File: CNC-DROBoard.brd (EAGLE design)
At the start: 99.1 x 85.1 mm, 50 parts, among them IC1 ATTINY2313A-PU, IC2 MAX7219CNG, IC3 MAX7219CNG, IC4 74HCT4053P

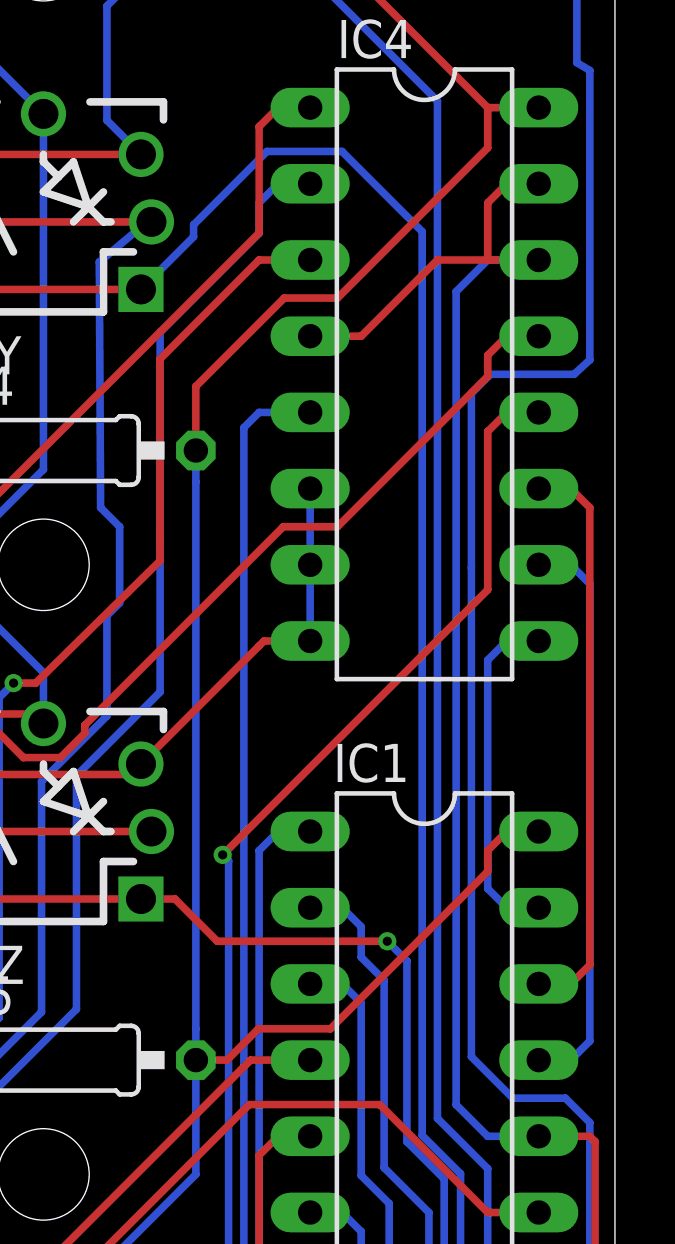
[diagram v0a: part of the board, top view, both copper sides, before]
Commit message: BUGFIX: 74LS4053 doesn't have the commons where you'd think it has - misleading symbol helped me mistake select inputs for common outputs - updated schematic, PCB update pending - this is probably not reworkable on a populated PCB. Will investigate reworkability of a blank PCB - contingency: dead-bug tehnique for the 4053 and onwards we go.
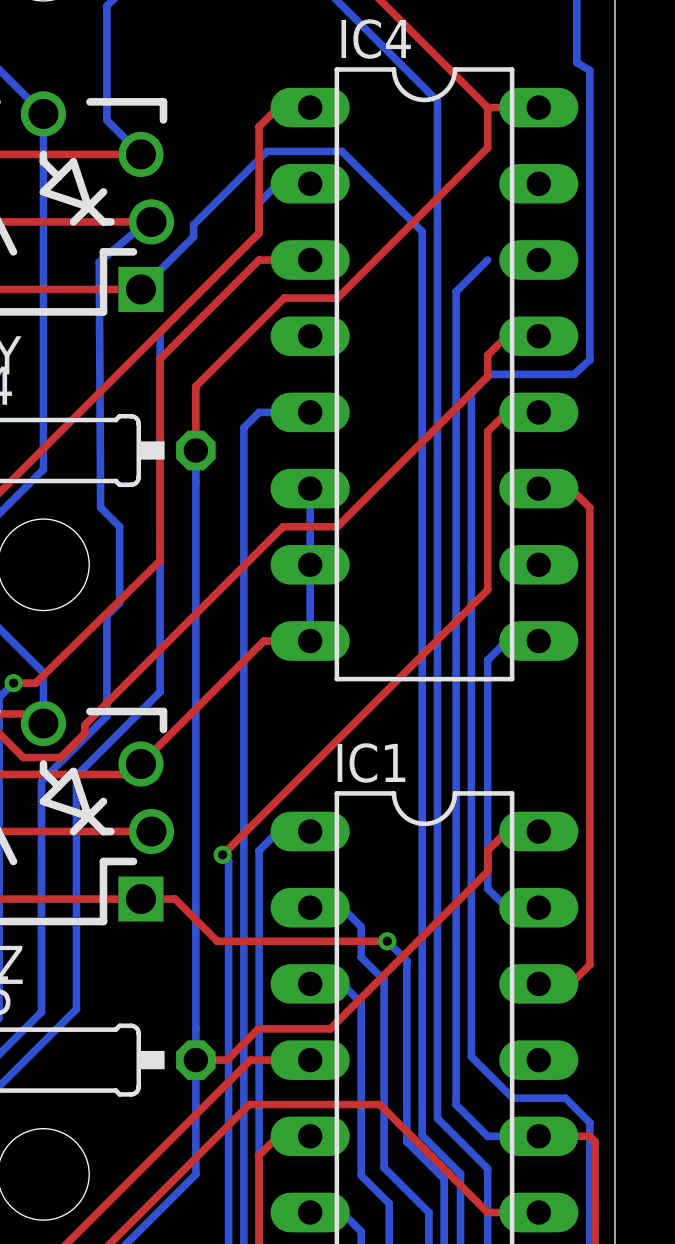
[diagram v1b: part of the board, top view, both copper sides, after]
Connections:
- net !SS: now also IC4.10, IC4.11, IC4.9; no longer IC4.14, IC4.15, IC4.4
- net MISO_INT: now also IC4.14; no longer IC4.11
- net MOSI_INT: now also IC4.15; no longer IC4.10
- net SCK_INT: now also IC4.4; no longer IC4.9
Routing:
- net MOSI_INT: track 19.2 -> 0.00 mm
- net !SS: track 96.5 -> 82.3 mm
- net MISO_INT: track 19.2 -> 18.1 mm
- net SCK_INT: track 11.5 -> 10.5 mm
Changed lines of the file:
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@@
 <?xml version="1.0" encoding="utf-8"?>
 <!DOCTYPE eagle SYSTEM "eagle.dtd">
-<eagle version="6.3">
+<eagle version="6.4">
 <drawing>
 <settings>
@@
 <contactref element="JBUS" pad="3"/>
 <contactref element="IC1" pad="16"/>
-<contactref element="IC4" pad="14"/>
-<contactref element="IC4" pad="15"/>
-<contactref element="IC4" pad="4"/>
 <wire x1="96.52" y1="22.86" x2="98.2219" y2="22.86" width="0.254" layer="1"/>
 <wire x1="71.12" y1="2.54" x2="72.4635" y2="1.1965" width="0.254" layer="1"/>
@@
 <wire x1="98.3977" y1="2.4874" x2="98.3977" y2="22.6842" width="0.254" layer="1"/>
 <wire x1="98.3977" y1="22.6842" x2="98.2219" y2="22.86" width="0.254" layer="1"/>
-<wire x1="96.52" y1="52.07" x2="94.8181" y2="52.07" width="0.254" layer="16"/>
 <wire x1="96.52" y1="22.86" x2="94.8181" y2="22.86" width="0.254" layer="16"/>
 <wire x1="94.8181" y1="22.86" x2="93.7656" y2="23.9125" width="0.254" layer="16"/>
 <wire x1="93.7656" y1="23.9125" x2="93.7656" y2="51.0175" width="0.254" layer="16"/>
 <wire x1="93.7656" y1="51.0175" x2="94.8181" y2="52.07" width="0.254" layer="16"/>
-<wire x1="94.8181" y1="52.07" x2="93.1419" y2="52.07" width="0.254" layer="1"/>
-<wire x1="93.1419" y1="52.07" x2="90.6019" y2="49.53" width="0.254" layer="1"/>
-<wire x1="96.52" y1="52.07" x2="94.8181" y2="52.07" width="0.254" layer="1"/>
-<wire x1="96.52" y1="54.61" x2="95.4531" y2="54.61" width="0.254" layer="1"/>
-<wire x1="95.4531" y1="54.61" x2="94.8181" y2="53.975" width="0.254" layer="1"/>
-<wire x1="94.8181" y1="53.975" x2="94.8181" y2="52.07" width="0.254" layer="1"/>
-<wire x1="88.9" y1="49.53" x2="90.6019" y2="49.53" width="0.254" layer="1"/>
+<contactref element="IC4" pad="9"/>
+<contactref element="IC4" pad="10"/>
+<contactref element="IC4" pad="11"/>
+<wire x1="96.52" y1="41.91" x2="96.52" y2="44.45" width="0" layer="19" extent="1-1"/>
+<wire x1="96.52" y1="39.37" x2="96.52" y2="41.91" width="0" layer="19" extent="1-1"/>
+<wire x1="93.7656" y1="51.0175" x2="96.52" y2="44.45" width="0" layer="19" extent="16-16"/>
 </signal>
 <signal name="!RESET">
@@
 <signal name="SCK_INT">
 <contactref element="IC1" pad="19"/>
-<contactref element="IC4" pad="9"/>
 <wire x1="94.8181" y1="38.735" x2="94.8181" y2="31.115" width="0.254" layer="16"/>
 <wire x1="94.8181" y1="31.115" x2="95.4531" y2="30.48" width="0.254" layer="16"/>
 <wire x1="95.4531" y1="30.48" x2="96.52" y2="30.48" width="0.254" layer="16"/>
-<wire x1="96.52" y1="39.37" x2="95.4531" y2="39.37" width="0.254" layer="16"/>
 <wire x1="95.4531" y1="39.37" x2="94.8181" y2="38.735" width="0.254" layer="16"/>
-</signal>
-<signal name="MOSI_INT">
-<contactref element="IC1" pad="17"/>
-<contactref element="IC4" pad="10"/>
-<wire x1="98.2219" y1="41.275" x2="98.2219" y2="26.035" width="0.254" layer="16"/>
-<wire x1="98.2219" y1="26.035" x2="97.5869" y2="25.4" width="0.254" layer="16"/>
-<wire x1="97.5869" y1="25.4" x2="96.52" y2="25.4" width="0.254" layer="16"/>
-<wire x1="96.52" y1="41.91" x2="97.5869" y2="41.91" width="0.254" layer="16"/>
-<wire x1="97.5869" y1="41.91" x2="98.2219" y2="41.275" width="0.254" layer="16"/>
+<contactref element="IC4" pad="4"/>
+<wire x1="95.4531" y1="39.37" x2="88.9" y2="49.53" width="0" layer="19" extent="16-16"/>
 </signal>
 <signal name="!SS_INT">
@@
 <signal name="MISO_INT">
 <contactref element="IC1" pad="18"/>
-<contactref element="IC4" pad="11"/>
 <wire x1="98.2219" y1="43.815" x2="98.2219" y2="28.575" width="0.254" layer="1"/>
 <wire x1="98.2219" y1="28.575" x2="97.5869" y2="27.94" width="0.254" layer="1"/>
 <wire x1="97.5869" y1="27.94" x2="96.52" y2="27.94" width="0.254" layer="1"/>
-<wire x1="96.52" y1="44.45" x2="97.5869" y2="44.45" width="0.254" layer="1"/>
 <wire x1="97.5869" y1="44.45" x2="98.2219" y2="43.815" width="0.254" layer="1"/>
+<contactref element="IC4" pad="14"/>
+<wire x1="97.5869" y1="44.45" x2="96.52" y2="52.07" width="0" layer="19" extent="1-1"/>
 </signal>
 <signal name="GPIO">
@@
 <wire x1="44.45" y1="17.78" x2="44.45" y2="19.4819" width="0.254" layer="1"/>
 </signal>
+<signal name="MOSI_INT">
+<contactref element="IC4" pad="15"/>
+<contactref element="IC1" pad="17"/>
+<wire x1="96.52" y1="25.4" x2="96.52" y2="54.61" width="0" layer="19" extent="1-1"/>
+</signal>
 </signals>

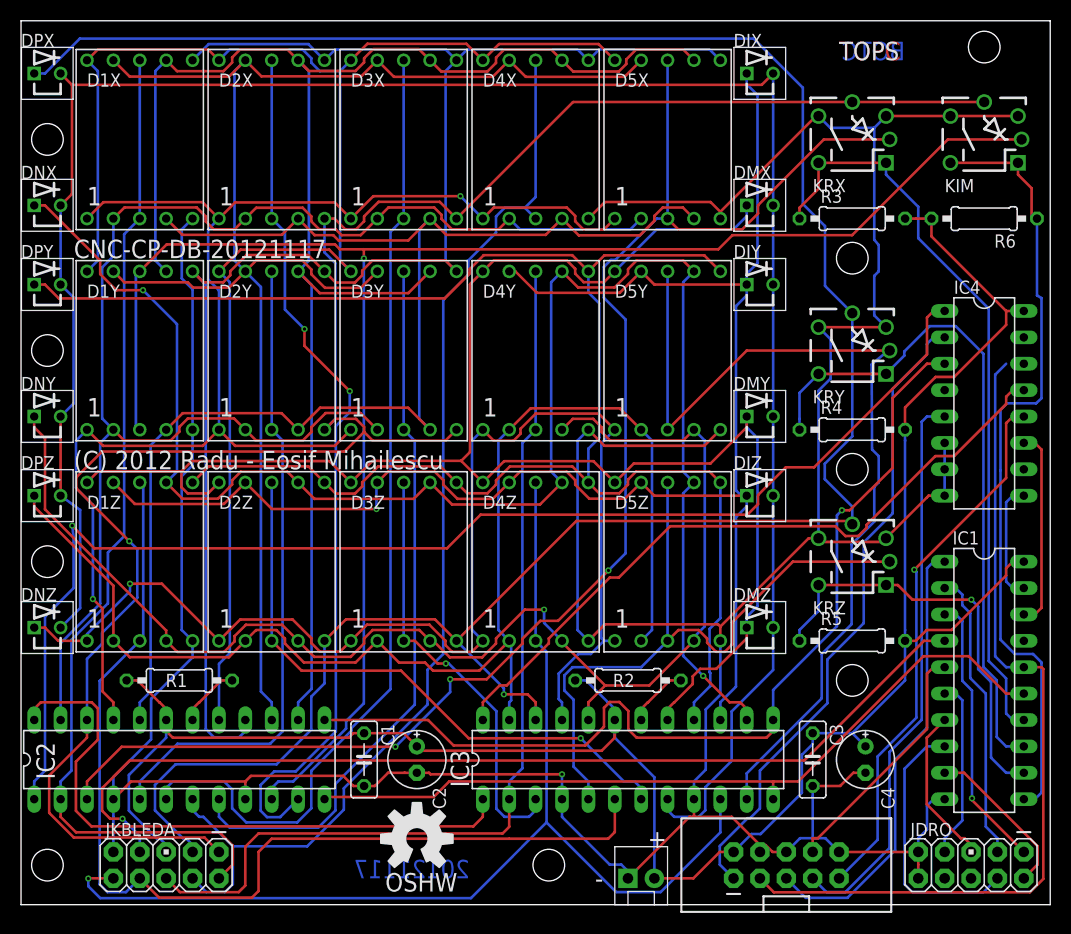
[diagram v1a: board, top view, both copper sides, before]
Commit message: BUGFIX: Same 4053 mistake fixed on Controls board as well UPDATE: 27k instead of 33k for Riset as all LEDs can handle 20mA at 2.1V - routed both DRO and Controls in FreeRouting - updated silkscreen/artwork to reflect new revision - still needs to fix DRU checks (FreeRouting always sees non-PTH holes smaller)
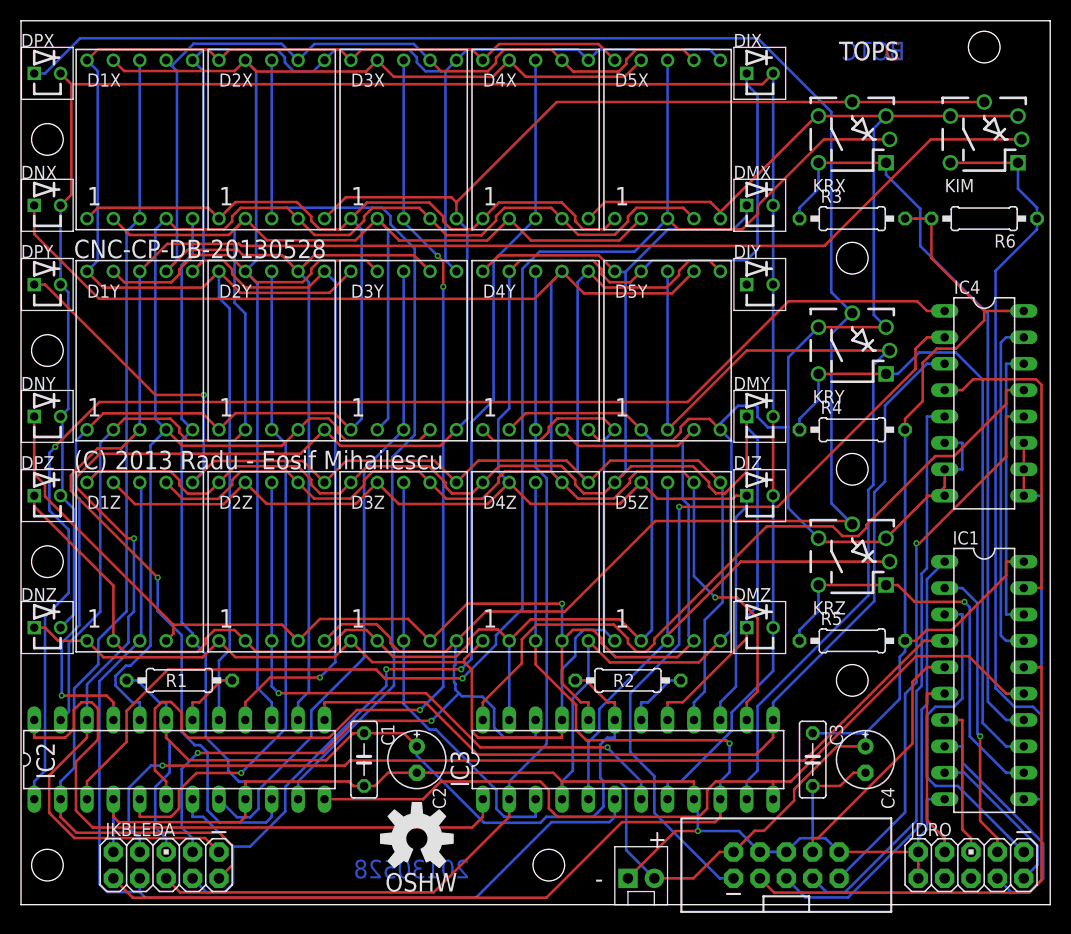
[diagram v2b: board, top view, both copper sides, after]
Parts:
- R1, R2: value 33k -> 27k
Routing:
- net MOSI_INT: track 0.00 -> 33.0 mm
- net SEGBB: track 174.5 -> 147.7 mm, vias 0 -> 1
- net SCK_INT: track 10.5 -> 31.2 mm
- net SEGBA: track 162.4 -> 180.4 mm, vias 2 -> 1
- net MOSI: track 62.3 -> 76.1 mm, vias 0 -> 1
- net VCC: track 200.6 -> 210.6 mm
- net SEGBE: track 122.9 -> 113.2 mm, vias 1 -> 0
- net MISO_INT: track 18.1 -> 27.5 mm
- net DIGA2: track 94.2 -> 103.6 mm, vias 0 -> 3
- net SEGBDP: track 227.5 -> 236.8 mm, vias 1 -> 2
- net SEGAA: track 160.0 -> 150.8 mm
- net DIGB6: track 67.2 -> 58.5 mm
- net GND: track 375.2 -> 382.7 mm
- net SEGBD: track 126.3 -> 118.9 mm
- net SEGAG: track 155.6 -> 148.3 mm
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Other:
- board text added: "(C) 2013 Radu - Eosif Mihailescu"
- board text added: "20130528"
- board text added: "CNC-CP-DB-20130528"
- board text removed: "(C) 2012 Radu - Eosif Mihailescu"
- board text removed: "20121117"
- board text removed: "CNC-CP-DB-20121117"
